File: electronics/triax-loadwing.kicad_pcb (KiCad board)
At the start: 2 copper layers, 60 x 30 mm, 52 parts, among them P1 CONN_01X06, P2 CONN_01X06, P3 CONN_01X06, P4 CONN_01X08, P5 JST_SH_4_RA, U1 NAU7802, U2 NAU7802, U3 NAU7802, U4 TCA9548A

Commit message: Routing complete
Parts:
- JP1, JP2, JP3: footprint Applidyne_Link:SJ1005-2N -> Applidyne_Link:SJ1608-2N
- moved JP1 6.28 mm to (164.5, 87.8), turned to 270 degrees
- moved JP3 4.20 mm to (170.0, 87.8), turned to 270 degrees
- moved JP2 1.15 mm to (167.3, 87.8), turned to 270 degrees
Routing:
- net READY_1: track 3.68 -> 52.9 mm, vias 1 -> 3
- net ~RESET: track 22.4 -> 71.2 mm, vias 0 -> 3
- net READY_2: track 3.43 -> 35.0 mm, vias 1 -> 3
- net +3.3V: track 24.1 -> 54.3 mm, vias 0 -> 6
- net SDA: track 24.3 -> 47.6 mm, vias 0 -> 2
- net SCL: track 19.2 -> 39.9 mm, vias 0 -> 2
- net GND: track 83.8 -> 98.3 mm, vias 19 -> 23
- net Net-(JP3-Pad1): track 13.3 -> 23.7 mm, vias 2 -> 4
- net READY_3: track 3.93 -> 13.6 mm
- net Net-(JP2-Pad1): track 11.4 -> 18.6 mm, vias 0 -> 2
- net Net-(JP1-Pad1): track 14.9 -> 19.3 mm, vias 0 -> 2
- net Net-(R15-Pad2): track 27.5 -> 26.3 mm
- net Net-(R12-Pad1): track 27.4 -> 26.4 mm
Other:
- board text removed: "Qwiic"

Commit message: Cosmetics final pass
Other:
- board text added: "0"
- board text added: "1"
- board text added: "2"
- board text added: "V1.0"
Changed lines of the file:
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@@
   (general
     (thickness 1.6)
-    (drawings 90)
-    (tracks 492)
+    (drawings 94)
+    (tracks 500)
     (zones 0)
     (modules 52)
@@
     )
   )
+  (gr_text V1.0 (at 138.1 88.1) (layer B.SilkS)
+    (effects (font (size 1 1) (thickness 0.15)) (justify mirror))
+  )
+  (gr_text 2 (at 170 85.5) (layer F.SilkS)
+    (effects (font (size 1 1) (thickness 0.15)))
+  )
+  (gr_text 1 (at 167.3 85.5) (layer F.SilkS)
+    (effects (font (size 1 1) (thickness 0.15)))
+  )
+  (gr_text 0 (at 164.5 85.5) (layer F.SilkS)
+    (effects (font (size 1 1) (thickness 0.15)))
+  )
   (gr_line (start 190.1 71.7) (end 190.1 72.1) (layer B.SilkS) (width 0.12))
   (gr_line (start 190.1 75.7) (end 190.1 76.1) (layer B.SilkS) (width 0.12))
@@
   (segment (start 145.325 71.525) (end 145.325 68.6) (width 0.25) (layer F.Cu) (net 3))
   (segment (start 147 66.775) (end 145 66.775) (width 0.25) (layer F.Cu) (net 3))
-  (segment (start 148.5 64.5) (end 148.5 62) (width 0.25) (layer F.Cu) (net 3))
-  (segment (start 148.75 64.75) (end 148.5 64.5) (width 0.25) (layer F.Cu) (net 3))
-  (segment (start 148.75 69.5) (end 148.75 64.75) (width 0.25) (layer F.Cu) (net 3))
-  (segment (start 149.135 69.885) (end 148.75 69.5) (width 0.25) (layer F.Cu) (net 3))
-  (segment (start 149.135 71.525) (end 149.135 69.885) (width 0.25) (layer F.Cu) (net 3))
   (segment (start 163.825 68.6) (end 163.725 68.5) (width 0.25) (layer F.Cu) (net 3))
   (segment (start 163.825 71.525) (end 163.825 68.6) (width 0.25) (layer F.Cu) (net 3))
@@
   (segment (start 162.555 77.754996) (end 163.200005 78.400001) (width 0.25) (layer F.Cu) (net 3))
   (segment (start 163.200005 78.400001) (end 163.600004 78.8) (width 0.25) (layer F.Cu) (net 3))
+  (segment (start 148.75 69.5) (end 148.75 62.25) (width 0.25) (layer F.Cu) (net 3))
+  (segment (start 148.75 62.25) (end 148.5 62) (width 0.25) (layer F.Cu) (net 3))
+  (segment (start 149.135 69.885) (end 148.75 69.5) (width 0.25) (layer F.Cu) (net 3))
+  (segment (start 149.135 71.525) (end 149.135 69.885) (width 0.25) (layer F.Cu) (net 3))
   (segment (start 180.42 63.645) (end 182 65.225) (width 0.25) (layer F.Cu) (net 4))
   (segment (start 180.42 62) (end 180.42 63.645) (width 0.25) (layer F.Cu) (net 4))
@@
   (segment (start 159.9179 85.950011) (end 159.25 85.282111) (width 0.25) (layer F.Cu) (net 17))
   (segment (start 161.950011 85.950011) (end 159.9179 85.950011) (width 0.25) (layer F.Cu) (net 17))
-  (segment (start 156.58 83.75) (end 155.96 83.75) (width 0.25) (layer F.Cu) (net 18))
-  (segment (start 155.96 83.75) (end 155.5 83.75) (width 0.25) (layer F.Cu) (net 18))
-  (via (at 155.5 83.75) (size 0.8) (drill 0.4) (layers F.Cu B.Cu) (net 18))
   (segment (start 166.200011 85.950011) (end 165.549989 85.950011) (width 0.25) (layer F.Cu) (net 17))
   (segment (start 167.3 87.05) (end 166.200011 85.950011) (width 0.25) (layer F.Cu) (net 17))
@@
   (segment (start 167.3 87.125) (end 168.174996 87.125) (width 0.25) (layer F.Cu) (net 17))
   (segment (start 173.4 86.9) (end 168.799996 86.9) (width 0.25) (layer B.Cu) (net 17))
+  (segment (start 156.58 83.75) (end 155.96 83.75) (width 0.25) (layer F.Cu) (net 18))
+  (segment (start 155.96 83.75) (end 155.5 83.75) (width 0.25) (layer F.Cu) (net 18))
+  (via (at 155.5 83.75) (size 0.8) (drill 0.4) (layers F.Cu B.Cu) (net 18))
   (segment (start 170 87.125) (end 170 85.9) (width 0.25) (layer F.Cu) (net 18))
   (via (at 174.2 86.1) (size 0.8) (drill 0.4) (layers F.Cu B.Cu) (net 18))
@@
   (segment (start 166.1 78.7) (end 164.9 78.7) (width 0.25) (layer F.Cu) (net 32))
   (segment (start 166.365 76.475) (end 166.365 78.435) (width 0.25) (layer F.Cu) (net 32))
-  (segment (start 152.90488 75.1) (end 153.1651 74.83978) (width 0.25) (layer F.Cu) (net 32))
-  (segment (start 142.900006 75.1) (end 152.90488 75.1) (width 0.25) (layer F.Cu) (net 32))
   (via (at 153.1651 74.83978) (size 0.8) (drill 0.4) (layers F.Cu B.Cu) (net 32))
   (segment (start 156.2 77.5) (end 153.53978 74.83978) (width 0.25) (layer B.Cu) (net 32))
   (segment (start 153.53978 74.83978) (end 153.1651 74.83978) (width 0.25) (layer B.Cu) (net 32))
+  (segment (start 152.125 74.625) (end 152.4 74.9) (width 0.25) (layer F.Cu) (net 32))
+  (segment (start 144.775 74.625) (end 152.125 74.625) (width 0.25) (layer F.Cu) (net 32))
+  (segment (start 144.5 74.9) (end 144.775 74.625) (width 0.25) (layer F.Cu) (net 32))
+  (segment (start 153.10488 74.9) (end 153.1651 74.83978) (width 0.25) (layer F.Cu) (net 32))
+  (segment (start 143.100006 74.9) (end 144.5 74.9) (width 0.25) (layer F.Cu) (net 32))
+  (segment (start 152.4 74.9) (end 153.10488 74.9) (width 0.25) (layer F.Cu) (net 32))
+  (segment (start 142.900006 75.1) (end 143.100006 74.9) (width 0.25) (layer F.Cu) (net 32))
   (segment (start 147.865 76.475) (end 147.865 78.135) (width 0.25) (layer F.Cu) (net 35))
   (segment (start 147.865 78.135) (end 147.5 78.5) (width 0.25) (layer F.Cu) (net 35))
@@
   (segment (start 138.24 73.4) (end 143 73.4) (width 0.25) (layer B.Cu) (net 50))
   (segment (start 137 72.16) (end 138.24 73.4) (width 0.25) (layer B.Cu) (net 50))
-  (segment (start 143 73.4) (end 151.4 73.4) (width 0.25) (layer F.Cu) (net 50))
   (via (at 151.4 73.4) (size 0.8) (drill 0.4) (layers F.Cu B.Cu) (net 50))
   (via (at 179 84.8) (size 0.8) (drill 0.4) (layers F.Cu B.Cu) (net 50))
@@
   (segment (start 171.7 77.2) (end 157.7 77.2) (width 0.25) (layer B.Cu) (net 50))
   (segment (start 156.6 78.3) (end 155.6 78.3) (width 0.25) (layer B.Cu) (net 50))
+  (segment (start 150.8 73.4) (end 151.4 73.4) (width 0.25) (layer F.Cu) (net 50))
+  (segment (start 145.02498 73.72498) (end 150.47502 73.72498) (width 0.25) (layer F.Cu) (net 50))
+  (segment (start 144.7 73.4) (end 145.02498 73.72498) (width 0.25) (layer F.Cu) (net 50))
+  (segment (start 150.47502 73.72498) (end 150.8 73.4) (width 0.25) (layer F.Cu) (net 50))
+  (segment (start 143 73.4) (end 144.7 73.4) (width 0.25) (layer F.Cu) (net 50))
   (segment (start 140.5 87.5) (end 142.25 87.5) (width 0.25) (layer F.Cu) (net 51))
   (segment (start 142.25 87.5) (end 143.025 86.725) (width 0.25) (layer F.Cu) (net 51))
@@
   (segment (start 141.845 86.5) (end 142.12 86.225) (width 0.25) (layer F.Cu) (net 52))
   (segment (start 140.5 86.5) (end 141.845 86.5) (width 0.25) (layer F.Cu) (net 52))
-  (segment (start 138.4 82.7) (end 138.3 82.7) (width 0.25) (layer B.Cu) (net 52))
-  (segment (start 141.925 86.225) (end 138.4 82.7) (width 0.25) (layer B.Cu) (net 52))
-  (segment (start 142.12 86.225) (end 141.925 86.225) (width 0.25) (layer B.Cu) (net 52))
+  (segment (start 138.9 82.7) (end 138.3 82.7) (width 0.25) (layer B.Cu) (net 52))
+  (segment (start 142.12 85.92) (end 138.9 82.7) (width 0.25) (layer B.Cu) (net 52))
+  (segment (start 142.12 86.225) (end 142.12 85.92) (width 0.25) (layer B.Cu) (net 52))
   (segment (start 193.12 63.63) (end 193.12 62) (width 0.3) (layer F.Cu) (net 53))
   (segment (start 189.945 66.805) (end 193.12 63.63) (width 0.3) (layer F.Cu) (net 53))

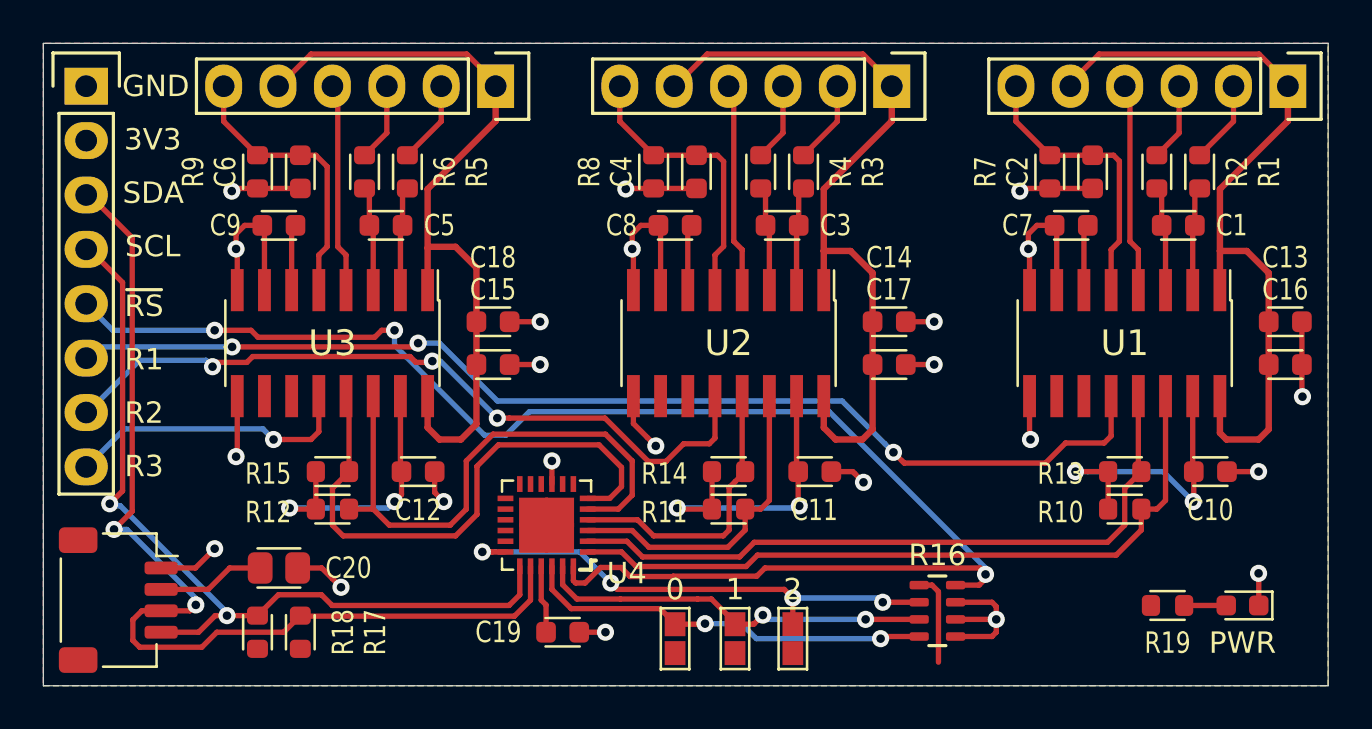
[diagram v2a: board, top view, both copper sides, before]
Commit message: Titleblocks, pcb manf notes
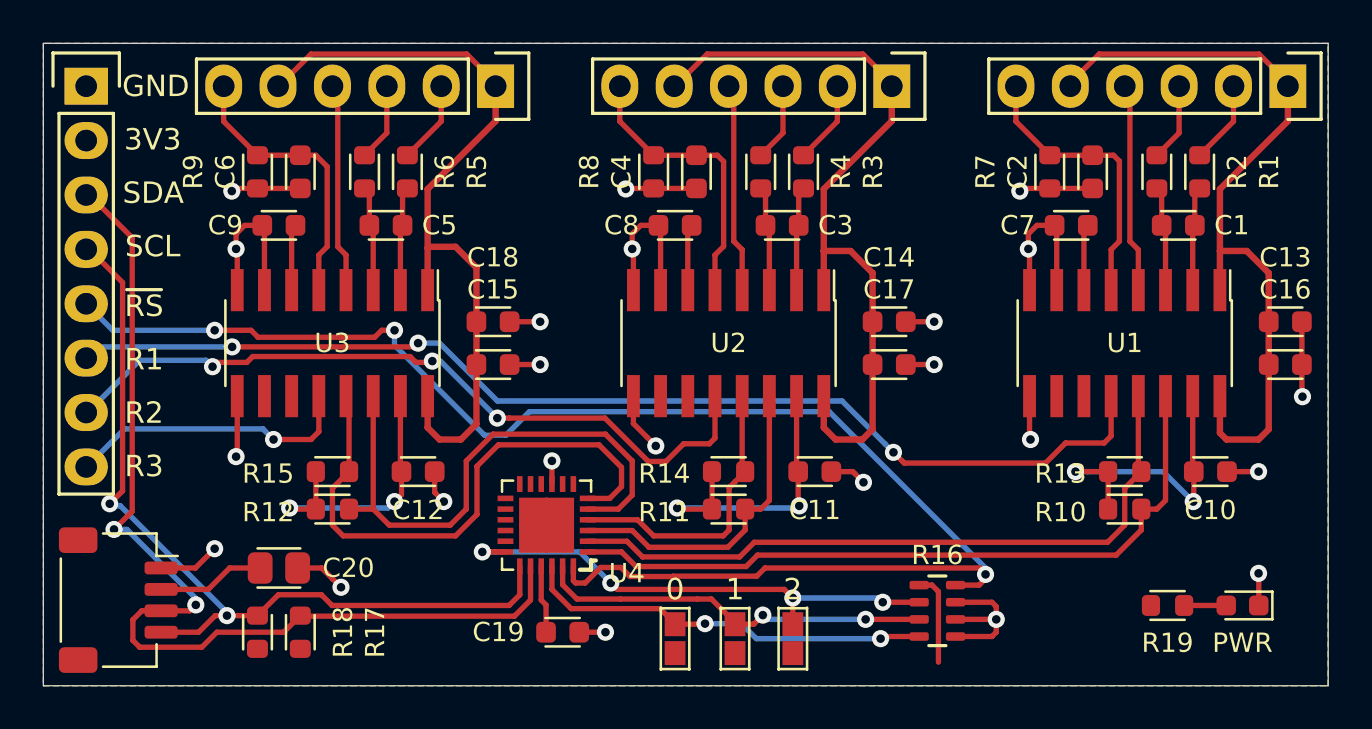
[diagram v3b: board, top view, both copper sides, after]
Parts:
- R16: value 10K_QUAD_ARRAY_1608M -> 10K_QUAD_1608M
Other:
- rule trace_min: 0.2 -> 0.25
- board text added: "Board Stackup 2-layer, 1.6mm thick 60 x 30 mm size 35um (1oz) copper layers ENIG surface finish White silkscreen Blue soldermask Min via drill: 0.4mm Min track thickness: 0.25mm Min clearance: 0.25mm"
- board text added: "CH1"
- board text added: "CH2"
- board text added: "CH3"
